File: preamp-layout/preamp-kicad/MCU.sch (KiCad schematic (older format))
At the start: 0 parts

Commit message: general layout work
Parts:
- added D?: LED, symbol Device:LED
- added J?: Conn_01x02_Female, symbol Connector:Conn_01x02_Female
- added J?: Conn_01x02_Male, symbol Connector:Conn_01x02_Male
- added R?: 330R, symbol Device:R
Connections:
- new net: D?.2 (A), R?.2
- new net +5V: J?.1 (Pin_1), J?.1 (Pin_1), R?.1
- new net GNDD: D?.1 (K), J?.2 (Pin_2), J?.2 (Pin_2)
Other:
- note added: "PWR, monitoring"
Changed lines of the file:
@@
 $Descr A4 11693 8268
 encoding utf-8
-Sheet 9 11
+Sheet 7 13
 Title ""
 Date ""
@@
 Text HLabel 4300 4400 0    50   Output ~ 0
 CS_IO
+Text GLabel 9550 4150 1    50   UnSpc ~ 0
++5V
+$Comp
+L power:GNDD #PWR?
+U 1 1 63AD6B0E
+P 9550 5050
+AR Path="/5E2D8DA2/63AD6B0E" Ref="#PWR?"  Part="1"
+AR Path="/619FA14B/63AD6B0E" Ref="#PWR?"  Part="1"
+F 0 "#PWR?" H 9550 4800 50  0001 C CNN
+F 1 "GNDD" H 9554 4895 50  0000 C CNN
+F 2 "" H 9550 5050 50  0001 C CNN
+F 3 "" H 9550 5050 50  0001 C CNN
+	1    9550 5050
+	1    0    0    -1
+$EndComp
+$Comp
+L Device:R R?
+U 1 1 63AD6B14
+P 9550 4400
+AR Path="/5E2D8DA2/63AD6B14" Ref="R?"  Part="1"
+AR Path="/63AD6B14" Ref="R?"  Part="1"
+AR Path="/619FA14B/63AD6B14" Ref="R?"  Part="1"
+F 0 "R?" V 9343 4400 50  0000 C CNN
+F 1 "330R" V 9434 4400 50  0000 C CNN
+F 2 "" V 9480 4400 50  0001 C CNN
+F 3 "~" H 9550 4400 50  0001 C CNN
+	1    9550 4400
+	1    0    0    -1
+$EndComp
+$Comp
+L Device:LED D?
+U 1 1 63AD6B1A
+P 9550 4800
+AR Path="/5E2D8DA2/63AD6B1A" Ref="D?"  Part="1"
+AR Path="/619FA14B/63AD6B1A" Ref="D?"  Part="1"
+F 0 "D?" V 9589 4683 50  0000 R CNN
+F 1 "LED" V 9498 4683 50  0000 R CNN
+F 2 "" H 9550 4800 50  0001 C CNN
+F 3 "~" H 9550 4800 50  0001 C CNN
+	1    9550 4800
+	0    -1   -1   0
+$EndComp
+Wire Wire Line
+	9550 4150 9550 4250
+Wire Wire Line
+	9550 4550 9550 4650
+Wire Wire Line
+	9550 4950 9550 5050
+$Comp
+L power:GNDD #PWR?
+U 1 1 63AD6B23
+P 9500 3300
+AR Path="/5E2D8DA2/63AD6B23" Ref="#PWR?"  Part="1"
+AR Path="/619FA14B/63AD6B23" Ref="#PWR?"  Part="1"
+F 0 "#PWR?" H 9500 3050 50  0001 C CNN
+F 1 "GNDD" H 9504 3145 50  0000 C CNN
+F 2 "" H 9500 3300 50  0001 C CNN
+F 3 "" H 9500 3300 50  0001 C CNN
+	1    9500 3300
+	1    0    0    -1
+$EndComp
+Wire Wire Line
+	9500 3200 9500 3300
+Wire Wire Line
+	9400 3100 9500 3100
+Text GLabel 9400 3100 0    50   UnSpc ~ 0
++5V
+$Comp
+L power:GNDD #PWR?
+U 1 1 63AD6B32
+P 9500 2750
+AR Path="/5E2D8DA2/63AD6B32" Ref="#PWR?"  Part="1"
+AR Path="/619FA14B/63AD6B32" Ref="#PWR?"  Part="1"
+F 0 "#PWR?" H 9500 2500 50  0001 C CNN
+F 1 "GNDD" H 9504 2595 50  0000 C CNN
+F 2 "" H 9500 2750 50  0001 C CNN
+F 3 "" H 9500 2750 50  0001 C CNN
+	1    9500 2750
+	1    0    0    -1
+$EndComp
+Wire Wire Line
+	9500 2650 9500 2750
+Wire Wire Line
+	9400 2550 9500 2550
+Text GLabel 9400 2550 0    50   UnSpc ~ 0
++5V
+$Comp
+L Connector:Conn_01x02_Female J?
+U 1 1 63AD6B3B
+P 9700 2550
+AR Path="/5E2D8DA2/63AD6B3B" Ref="J?"  Part="1"
+AR Path="/619FA14B/63AD6B3B" Ref="J?"  Part="1"
+F 0 "J?" H 9728 2526 50  0000 L CNN
+F 1 "Conn_01x02_Female" H 9728 2435 50  0000 L CNN
+F 2 "" H 9700 2550 50  0001 C CNN
+F 3 "~" H 9700 2550 50  0001 C CNN
+	1    9700 2550
+	1    0    0    -1
+$EndComp
+Text Notes 9250 2100 0    50   ~ 0
+PWR, monitoring
+$Comp
+L Connector:Conn_01x02_Male J?
+U 1 1 63AD6EFD
+P 9700 3100
+F 0 "J?" H 9672 3074 50  0000 R CNN
+F 1 "Conn_01x02_Male" H 9672 2983 50  0000 R CNN
+F 2 "" H 9700 3100 50  0001 C CNN
+F 3 "~" H 9700 3100 50  0001 C CNN
+	1    9700 3100
+	-1   0    0    -1
+$EndComp
+Text HLabel 6000 4000 2    50   Input ~ 0
+SEL_CLK
+Text HLabel 6000 4150 2    50   Input ~ 0
+SEL_DT
+Text HLabel 6000 4300 2    50   Input ~ 0
+SEL_SW
+Text HLabel 6000 4650 2    50   Input ~ 0
+VOL_CLK
+Text HLabel 6000 4800 2    50   Input ~ 0
+VOL_DT
+Text HLabel 6000 4950 2    50   Input ~ 0
+VOL_SW
+Text HLabel 6000 5100 2    50   Output ~ 0
+VOL_LED_DT
+Text HLabel 6000 4450 2    50   Output ~ 0
+SEL_LED_DT
 Text HLabel 4300 4600 0    50   Output ~ 0
-CS_VOL_LIGHT
+CS_FP
 Text HLabel 4300 4800 0    50   Output ~ 0
-CS_SELECT_LIGHT
-Text HLabel 4300 5000 0    50   Output ~ 0
-CS_VOL_ENCODER
-Text HLabel 4300 5200 0    50   Output ~ 0
-CS_SELECT_ENCODER
+CS_VOL
 $EndSCHEMATC

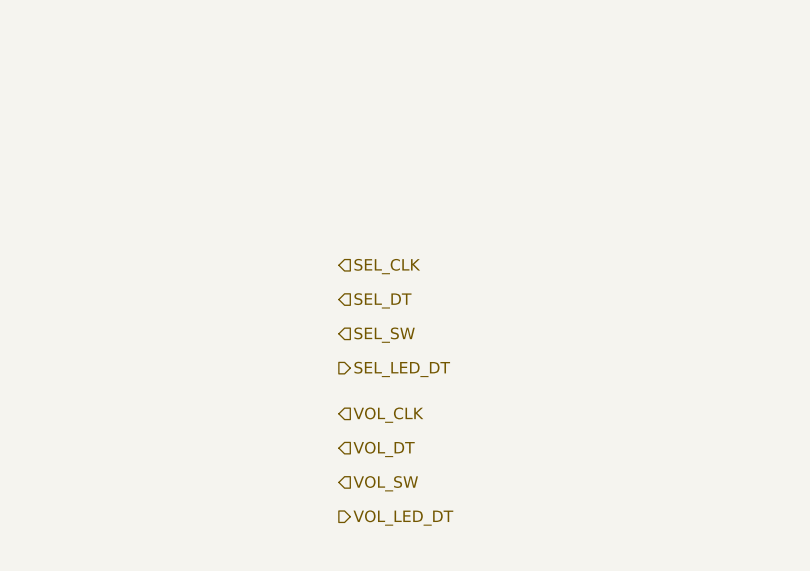
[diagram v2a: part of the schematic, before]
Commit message: Encoder, LED, front panel update
Removed hierarchical sheets for encoders, moved encoders to main sheet. Added switches for output select on front panel sheet. Added LEDs on front panel sheet but only as a symbol, only two instances currently present. Added LED data line between MCU and front panel.
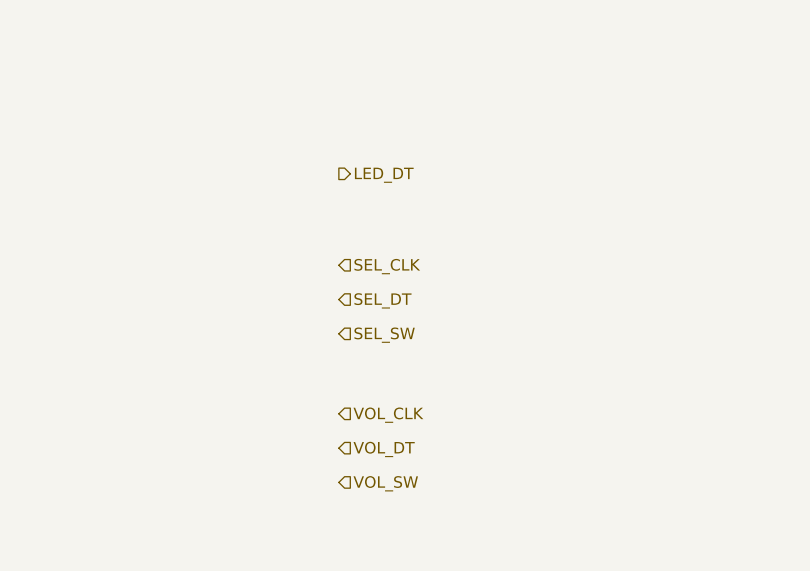
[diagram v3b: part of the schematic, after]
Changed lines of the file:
@@
 $Descr A4 11693 8268
 encoding utf-8
-Sheet 7 14
+Sheet 10 12
 Title ""
 Date ""
@@
 Text HLabel 6000 4950 2    50   Input ~ 0
 VOL_SW
-Text HLabel 6000 5100 2    50   Output ~ 0
-VOL_LED_DT
-Text HLabel 6000 4450 2    50   Output ~ 0
-SEL_LED_DT
 Text HLabel 4300 4600 0    50   Output ~ 0
 CS_FP
 Text HLabel 4300 4800 0    50   Output ~ 0
 CS_VOL
+Text HLabel 6000 3600 2    50   Output ~ 0
+LED_DT
 $EndSCHEMATC

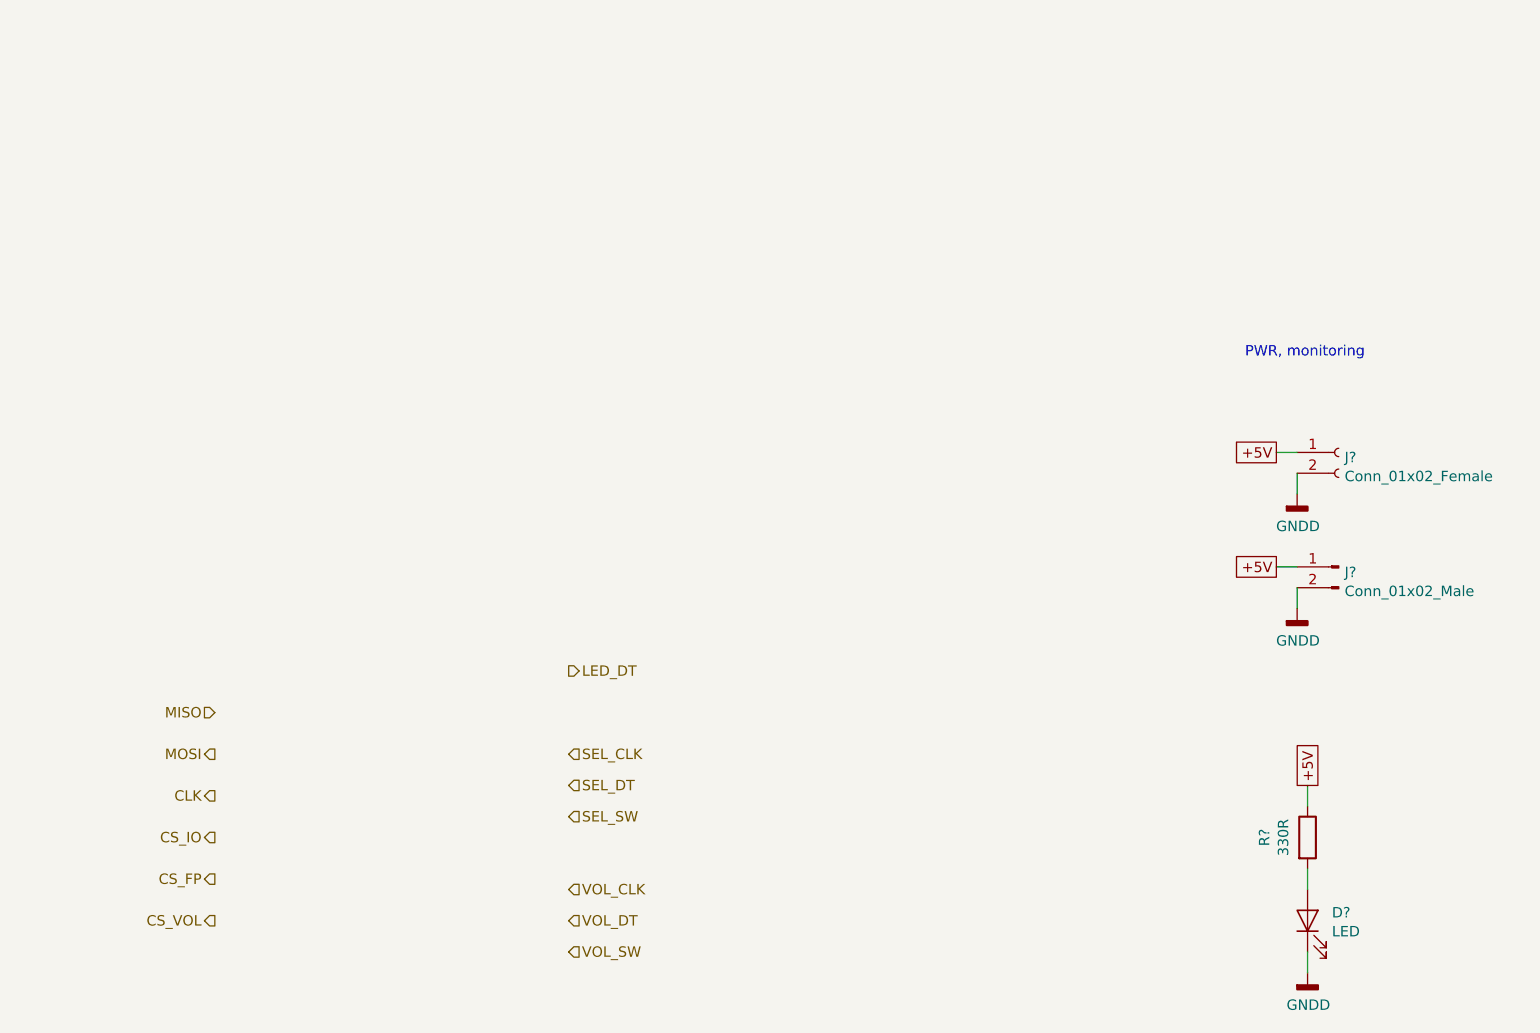
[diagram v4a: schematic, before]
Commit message: Updates
Minor Readme updates.
Schematic:
 - Bus connector lines replaced single wire connectors
 - Title block populated.
 - Power Supply updates.
 - Preliminary Front Panel.
 - Minor MCU work.
 -
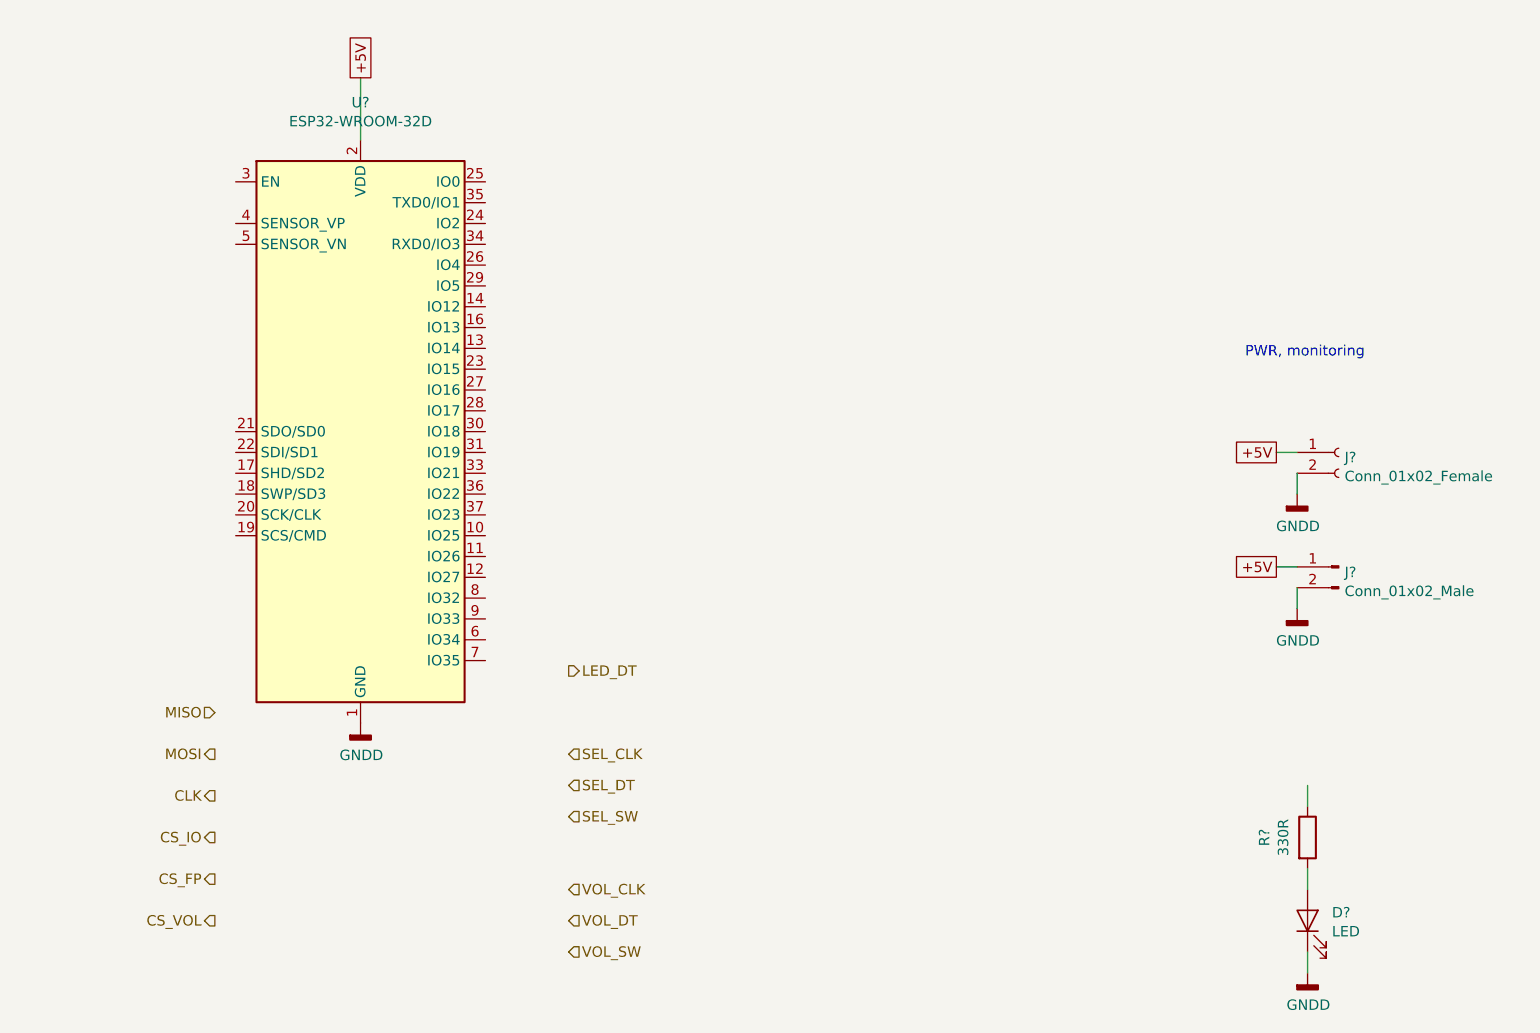
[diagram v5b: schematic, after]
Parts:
- added U?: ESP32-WROOM-32D, RF_Module:ESP32-WROOM-32, symbol RF_Module:ESP32-WROOM-32D
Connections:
- wire segments 7 -> 8
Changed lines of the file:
@@
 $Descr A4 11693 8268
 encoding utf-8
-Sheet 10 13
-Title ""
-Date ""
-Rev ""
+Sheet 8 13
+Title "Preamp MCU Board"
+Date "2020-01-09"
+Rev "A00"
 Comp ""
-Comment1 ""
-Comment2 ""
-Comment3 ""
-Comment4 ""
+Comment1 "creativecommons.org/licenses/by/4.0/"
+Comment2 "License: CC BY 4.0"
+Comment3 "github.com/SlurpyTurts/preamp"
+Comment4 "Author: Jordon Gerber"
 $EndDescr
 Text HLabel 4300 3800 0    50   Input ~ 0
@@
 Text HLabel 4300 4400 0    50   Output ~ 0
 CS_IO
-Text GLabel 9550 4150 1    50   UnSpc ~ 0
+Text GLabel 5000 750  1    50   UnSpc ~ 0
 +5V
 $Comp
@@
 Text HLabel 6000 3600 2    50   Output ~ 0
 LED_DT
+$Comp
+L RF_Module:ESP32-WROOM-32D U?
+U 1 1 5FF4D990
+P 5000 2450
+F 0 "U?" H 5000 4031 50  0000 C CNN
+F 1 "ESP32-WROOM-32D" H 5000 3940 50  0000 C CNN
+F 2 "RF_Module:ESP32-WROOM-32" H 5000 950 50  0001 C CNN
+F 3 "https://www.espressif.com/sites/default/files/documentation/esp32-wroom-32d_esp32-wroom-32u_datasheet_en.pdf" H 4700 2500 50  0001 C CNN
+	1    5000 2450
+	1    0    0    -1
+$EndComp
+Wire Wire Line
+	5000 750  5000 1050
+$Comp
+L power:GNDD #PWR?
+U 1 1 5FF5213F
+P 5000 3850
+AR Path="/5E2D8DA2/5FF5213F" Ref="#PWR?"  Part="1"
+AR Path="/619FA14B/5FF5213F" Ref="#PWR?"  Part="1"
+F 0 "#PWR?" H 5000 3600 50  0001 C CNN
+F 1 "GNDD" H 5004 3695 50  0000 C CNN
+F 2 "" H 5000 3850 50  0001 C CNN
+F 3 "" H 5000 3850 50  0001 C CNN
+	1    5000 3850
+	1    0    0    -1
+$EndComp
 $EndSCHEMATC

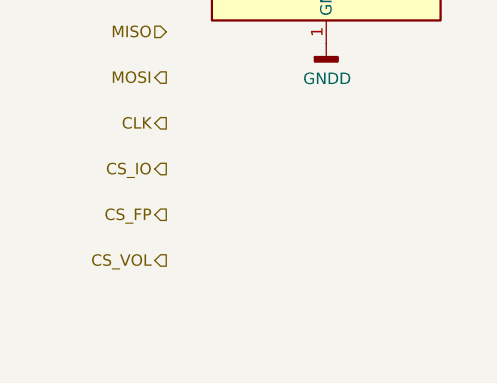
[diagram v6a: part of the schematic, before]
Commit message: VCA gain control
Removed MDAC volume control and gain stage, replaced with VCA gain stage.
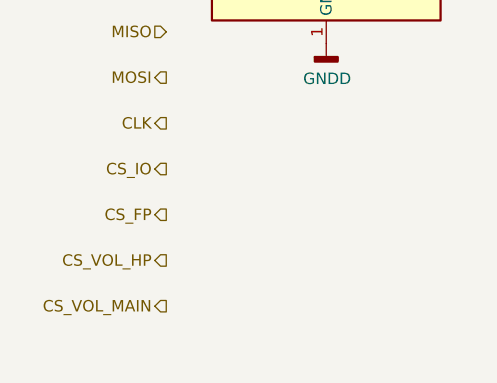
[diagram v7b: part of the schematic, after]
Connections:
- net labels added: CS_VOL_HP, CS_VOL_MAIN
- net labels removed: CS_VOL
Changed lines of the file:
@@
 $Descr A4 11693 8268
 encoding utf-8
-Sheet 8 14
+Sheet 7 13
 Title "Preamp MCU Board"
 Date "2020-01-09"
@@
 CS_FP
 Text HLabel 4300 4800 0    50   Output ~ 0
-CS_VOL
+CS_VOL_HP
 Text HLabel 6000 3600 2    50   Output ~ 0
 LED_DT
@@
 	1    0    0    -1
 $EndComp
+Text HLabel 4300 5000 0    50   Output ~ 0
+CS_VOL_MAIN
 $EndSCHEMATC

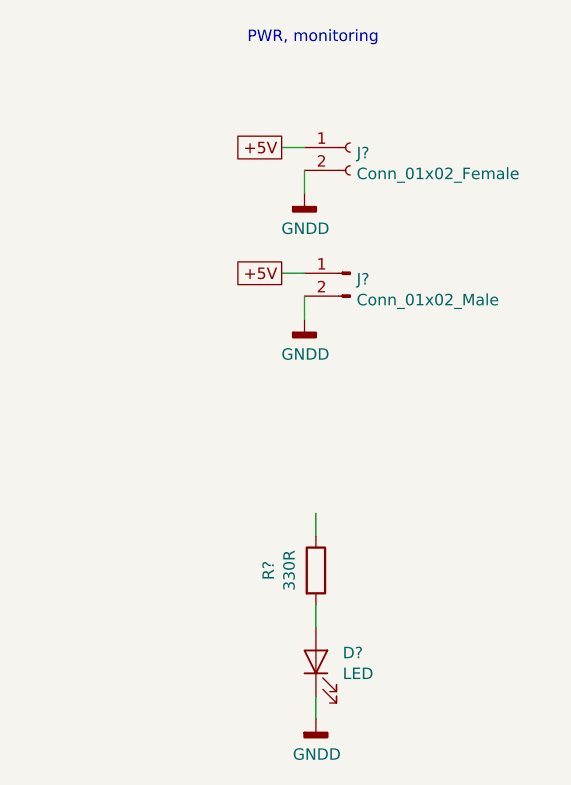
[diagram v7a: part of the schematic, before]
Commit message: Power conn cleanup
5V and 15V cleaned up on all sheets
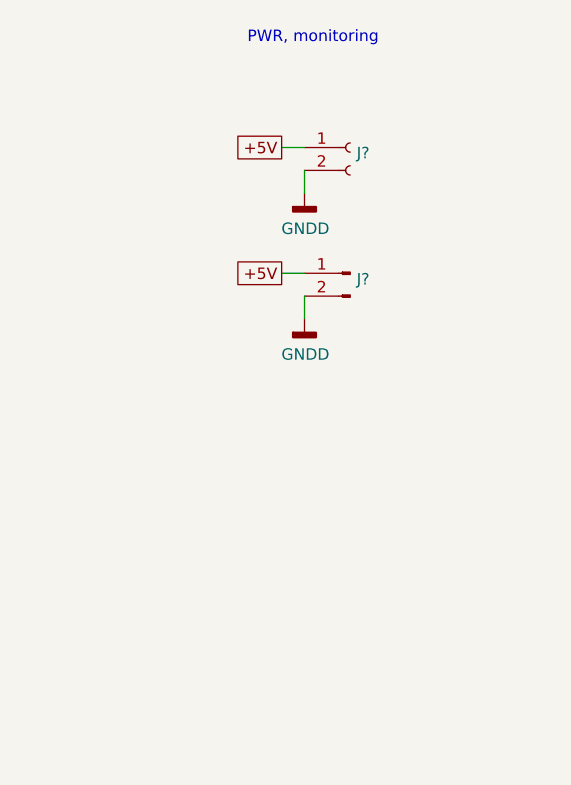
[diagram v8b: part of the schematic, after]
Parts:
- removed D?: LED, symbol Device:LED
- removed R?: 330R, symbol Device:R
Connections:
- wire segments 8 -> 5
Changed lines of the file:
@@
-$Comp
-L power:GNDD #PWR?
-U 1 1 63AD6B0E
-P 9550 5050
-AR Path="/5E2D8DA2/63AD6B0E" Ref="#PWR?"  Part="1"
-AR Path="/619FA14B/63AD6B0E" Ref="#PWR?"  Part="1"
-F 0 "#PWR?" H 9550 4800 50  0001 C CNN
-F 1 "GNDD" H 9554 4895 50  0000 C CNN
-F 2 "" H 9550 5050 50  0001 C CNN
-F 3 "" H 9550 5050 50  0001 C CNN
-	1    9550 5050
-	1    0    0    -1
-$EndComp
-$Comp
-L Device:R R?
-U 1 1 63AD6B14
-P 9550 4400
-AR Path="/5E2D8DA2/63AD6B14" Ref="R?"  Part="1"
-AR Path="/63AD6B14" Ref="R?"  Part="1"
-AR Path="/619FA14B/63AD6B14" Ref="R?"  Part="1"
-F 0 "R?" V 9343 4400 50  0000 C CNN
-F 1 "330R" V 9434 4400 50  0000 C CNN
-F 2 "" V 9480 4400 50  0001 C CNN
-F 3 "~" H 9550 4400 50  0001 C CNN
-	1    9550 4400
-	1    0    0    -1
-$EndComp
-$Comp
-L Device:LED D?
-U 1 1 63AD6B1A
-P 9550 4800
-AR Path="/5E2D8DA2/63AD6B1A" Ref="D?"  Part="1"
-AR Path="/619FA14B/63AD6B1A" Ref="D?"  Part="1"
-F 0 "D?" V 9589 4683 50  0000 R CNN
-F 1 "LED" V 9498 4683 50  0000 R CNN
-F 2 "" H 9550 4800 50  0001 C CNN
-F 3 "~" H 9550 4800 50  0001 C CNN
-	1    9550 4800
-	0    -1   -1   0
-$EndComp
-Wire Wire Line
-	9550 4150 9550 4250
-Wire Wire Line
-	9550 4550 9550 4650
-Wire Wire Line
-	9550 4950 9550 5050
 $Comp
 L power:GNDD #PWR?
@@
 AR Path="/619FA14B/63AD6B3B" Ref="J?"  Part="1"
 F 0 "J?" H 9728 2526 50  0000 L CNN
-F 1 "Conn_01x02_Female" H 9728 2435 50  0000 L CNN
+F 1 "Conn_01x02_Female" H 9728 2435 50  0001 L CNN
 F 2 "" H 9700 2550 50  0001 C CNN
 F 3 "~" H 9700 2550 50  0001 C CNN
@@
 P 9700 3100
 F 0 "J?" H 9672 3074 50  0000 R CNN
-F 1 "Conn_01x02_Male" H 9672 2983 50  0000 R CNN
+F 1 "Conn_01x02_Male" H 9672 2983 50  0001 R CNN
 F 2 "" H 9700 3100 50  0001 C CNN
 F 3 "~" H 9700 3100 50  0001 C CNN
